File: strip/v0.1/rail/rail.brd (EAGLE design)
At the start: 11.2 x 68 mm, 4 parts

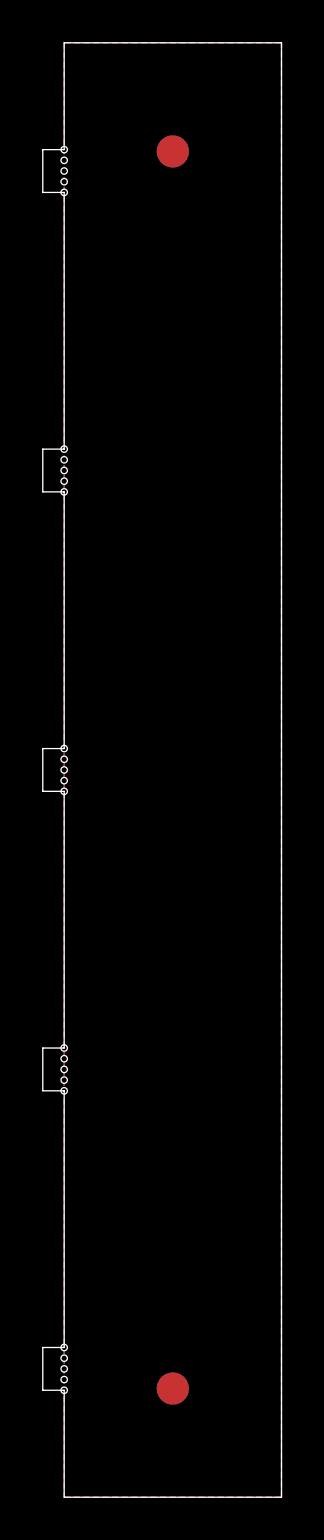
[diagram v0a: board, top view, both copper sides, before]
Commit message: Removed tabbing on the rails.
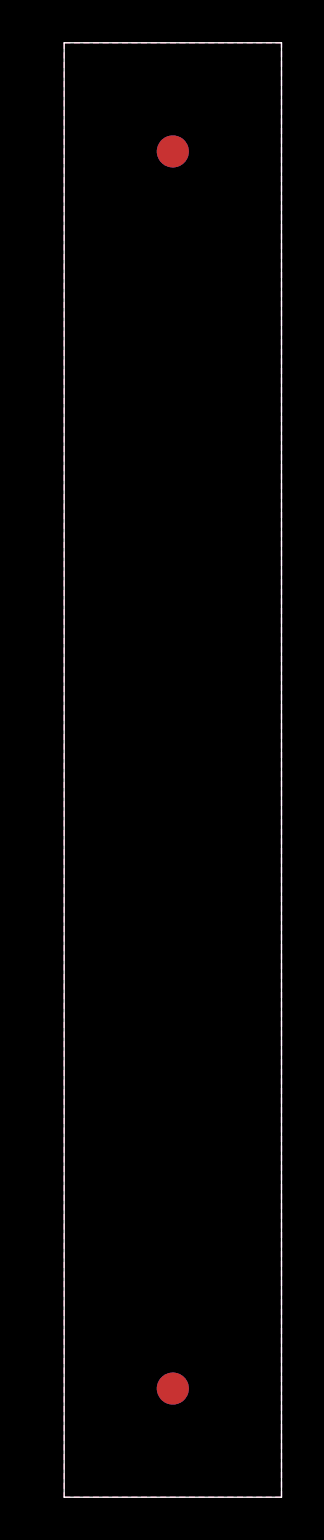
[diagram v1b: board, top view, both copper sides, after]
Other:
- board size 11.2 x 68 mm -> 10.2 x 68 mm
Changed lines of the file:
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@@
 <wire x1="10.16" y1="0" x2="10.16" y2="67.9958" width="0" layer="20"/>
 <wire x1="10.16" y1="67.9958" x2="0" y2="67.9958" width="0" layer="20"/>
-<wire x1="0" y1="67.9958" x2="0" y2="63" width="0" layer="20"/>
-<wire x1="0" y1="63" x2="-1" y2="63" width="0" layer="20"/>
-<wire x1="-1" y1="63" x2="-1" y2="61" width="0" layer="20"/>
-<wire x1="-1" y1="61" x2="0" y2="61" width="0" layer="20"/>
-<wire x1="0" y1="61" x2="0" y2="49" width="0" layer="20"/>
-<wire x1="0" y1="49" x2="-1" y2="49" width="0" layer="20"/>
-<wire x1="-1" y1="49" x2="-1" y2="47" width="0" layer="20"/>
-<wire x1="-1" y1="47" x2="0" y2="47" width="0" layer="20"/>
-<wire x1="0" y1="47" x2="0" y2="35" width="0" layer="20"/>
-<wire x1="0" y1="35" x2="-1" y2="35" width="0" layer="20"/>
-<wire x1="-1" y1="35" x2="-1" y2="33" width="0" layer="20"/>
-<wire x1="-1" y1="33" x2="0" y2="33" width="0" layer="20"/>
-<wire x1="0" y1="33" x2="0" y2="21" width="0" layer="20"/>
-<wire x1="0" y1="21" x2="-1" y2="21" width="0" layer="20"/>
-<wire x1="-1" y1="21" x2="-1" y2="19" width="0" layer="20"/>
-<wire x1="-1" y1="19" x2="0" y2="19" width="0" layer="20"/>
-<wire x1="0" y1="19" x2="0" y2="7" width="0" layer="20"/>
-<wire x1="0" y1="7" x2="-1" y2="7" width="0" layer="20"/>
-<wire x1="-1" y1="7" x2="-1" y2="5" width="0" layer="20"/>
-<wire x1="-1" y1="5" x2="0" y2="5" width="0" layer="20"/>
-<wire x1="0" y1="5" x2="0" y2="0" width="0" layer="20"/>
-<hole x="0" y="5" drill="0.3"/>
-<hole x="0" y="5.5" drill="0.3"/>
-<hole x="0" y="6" drill="0.3"/>
-<hole x="0" y="6.5" drill="0.3"/>
-<hole x="0" y="7" drill="0.3"/>
-<hole x="0" y="19.5" drill="0.3"/>
-<hole x="0" y="20.5" drill="0.3"/>
-<hole x="0" y="21" drill="0.3"/>
-<hole x="0" y="20" drill="0.3"/>
-<hole x="0" y="19" drill="0.3"/>
-<hole x="0" y="33" drill="0.3"/>
-<hole x="0" y="33.5" drill="0.3"/>
-<hole x="0" y="34" drill="0.3"/>
-<hole x="0" y="34.5" drill="0.3"/>
-<hole x="0" y="35" drill="0.3"/>
-<hole x="0" y="47" drill="0.3"/>
-<hole x="0" y="47.5" drill="0.3"/>
-<hole x="0" y="48" drill="0.3"/>
-<hole x="0" y="48.5" drill="0.3"/>
-<hole x="0" y="49" drill="0.3"/>
-<hole x="0" y="61.5" drill="0.3"/>
-<hole x="0" y="62" drill="0.3"/>
-<hole x="0" y="62.5" drill="0.3"/>
-<hole x="0" y="63" drill="0.3"/>
-<hole x="0" y="61" drill="0.3"/>
+<wire x1="0" y1="0" x2="0" y2="67.9958" width="0" layer="20"/>
 </plain>
 <attributes>
